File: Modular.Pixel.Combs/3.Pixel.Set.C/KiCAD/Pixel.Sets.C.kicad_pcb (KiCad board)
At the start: 2 copper layers, 78 x 78 mm, 19 parts

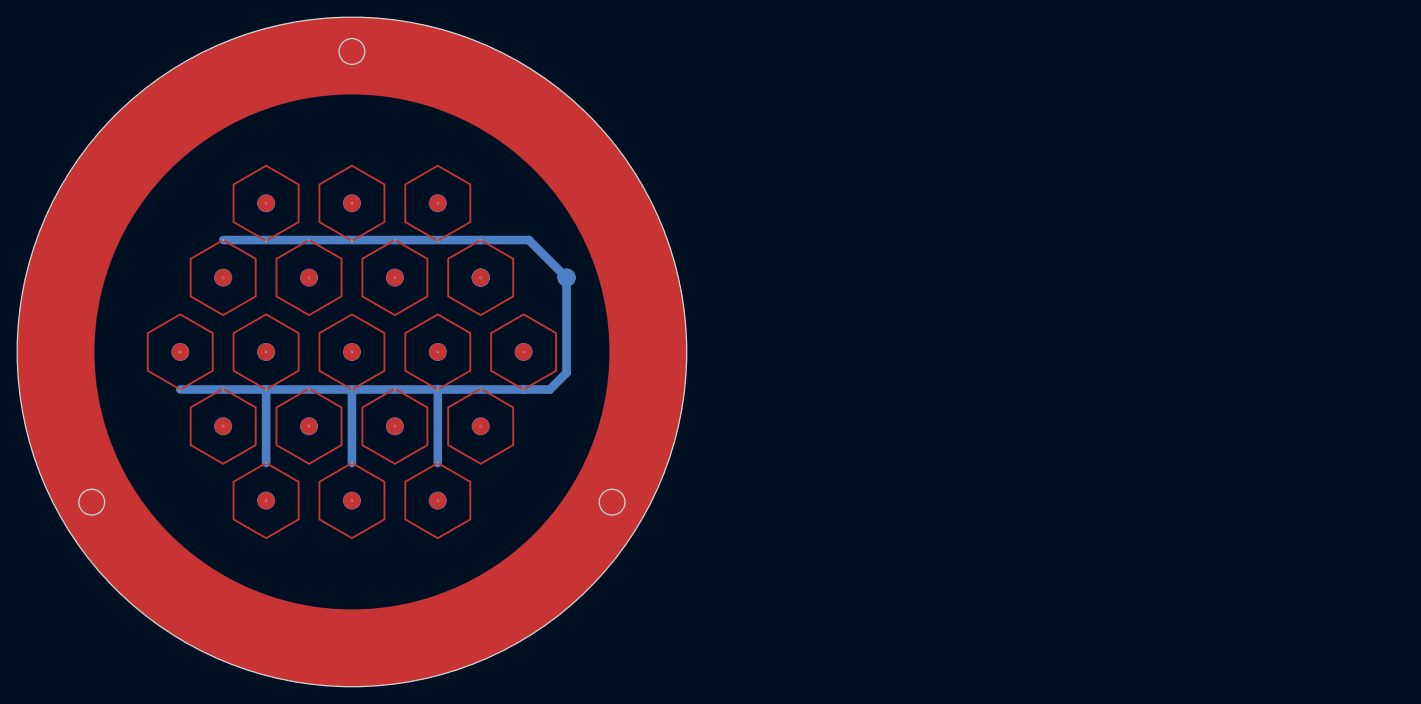
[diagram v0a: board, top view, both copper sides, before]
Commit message: Smoothed out Hexagon Pixels so that it Better Fits the Stencils
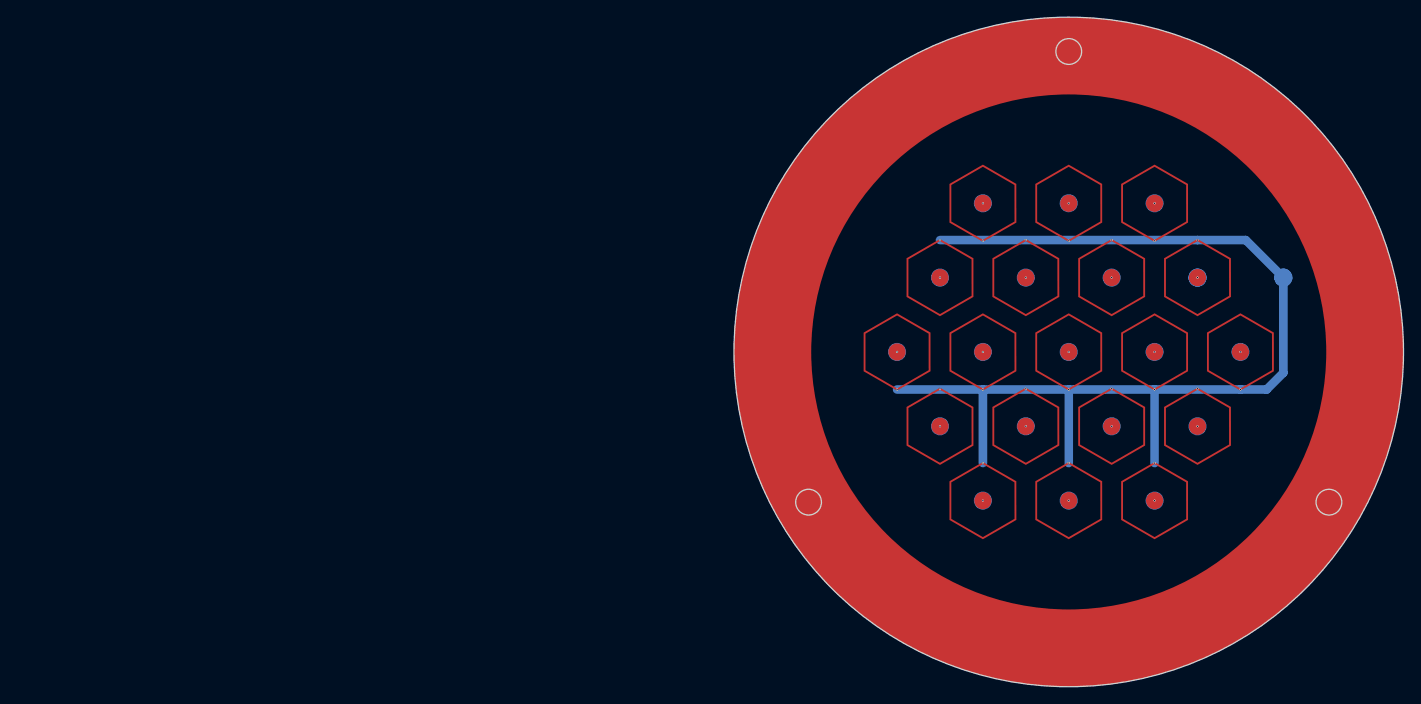
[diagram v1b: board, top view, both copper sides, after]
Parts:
- moved REF** 83.5 mm to (232.0, 58.3)
- moved REF**10 83.5 mm to (237.0, 49.6)
- moved REF**11 83.5 mm to (247.0, 49.6)
- moved REF**13 83.5 mm to (222.0, 41.0)
- moved REF**14 83.5 mm to (232.0, 41.0)
- moved REF**15 83.5 mm to (242.0, 41.0)
- moved REF**3 83.5 mm to (242.0, 58.3)
- moved REF**30 83.5 mm to (237.0, 67.0)
- moved REF**33 83.5 mm to (247.0, 67.0)
- moved REF**38 83.5 mm to (242.0, 75.6)
- moved REF**50 83.5 mm to (212.0, 58.3)
- moved REF**53 83.5 mm to (217.0, 49.6)
- moved REF**6 83.5 mm to (252.0, 58.3)
- moved REF**64 83.5 mm to (222.0, 58.3)
- moved REF**67 83.5 mm to (227.0, 67.0)
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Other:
- board text added: "Pixel Board C ::: May 2023 Alfredo Barajas Enriquez"
- board text removed: "Pixel Set C ::: May 2023 Alfredo Barajas Enriquez"

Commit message: Finalized Pixel Plane Design
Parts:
- removed the REF** at (232.0, 58.3)
- removed REF**10, REF**11, REF**13, REF**14, REF**15, REF**3, REF**30, REF**33, REF**38, REF**50, REF**53, REF**6, REF**64, REF**67, REF**68, REF**71, REF**80, REF**9: Hex.Tile.Solid.G.Dot, Hex:Hex.Tile.Solid.G.Dot
- added REF**: Hex.Tile.Solid.G.Dot, 1.Hex:Hex.Tile.Solid.G.Dot, F.Cu at (222.0, 41.0)
- added REF**: Hex.Tile.Solid.G.Dot, 1.Hex:Hex.Tile.Solid.G.Dot, F.Cu at (252.0, 58.3)
- added REF**: Hex.Tile.Solid.G.Dot, 1.Hex:Hex.Tile.Solid.G.Dot, F.Cu at (247.0, 49.6)
- added REF**: Hex.Tile.Solid.G.Dot, 1.Hex:Hex.Tile.Solid.G.Dot, F.Cu at (242.0, 58.3)
- added REF**: Hex.Tile.Solid.G.Dot, 1.Hex:Hex.Tile.Solid.G.Dot, F.Cu at (212.0, 58.3)
- added REF**: Hex.Tile.Solid.G.Dot, 1.Hex:Hex.Tile.Solid.G.Dot, F.Cu at (237.0, 67.0)
- added REF**: Hex.Tile.Solid.G.Dot, 1.Hex:Hex.Tile.Solid.G.Dot, F.Cu at (242.0, 41.0)
- added REF**: Hex.Tile.Solid.G.Dot, 1.Hex:Hex.Tile.Solid.G.Dot, F.Cu at (227.0, 49.6)
- added REF**: Hex.Tile.Solid.G.Dot, 1.Hex:Hex.Tile.Solid.G.Dot, F.Cu at (232.0, 41.0)
- added REF**: Hex.Tile.Solid.G.Dot, 1.Hex:Hex.Tile.Solid.G.Dot, F.Cu at (222.0, 75.6)
- added REF**: Hex.Tile.Solid.G.Dot, 1.Hex:Hex.Tile.Solid.G.Dot, F.Cu at (222.0, 58.3)
- added REF**: Hex.Tile.Solid.G.Dot, 1.Hex:Hex.Tile.Solid.G.Dot, F.Cu at (217.0, 49.6)
- added REF**: Hex.Tile.Solid.G.Dot, 1.Hex:Hex.Tile.Solid.G.Dot, F.Cu at (232.0, 58.3)
- added REF**: Hex.Tile.Solid.G.Dot, 1.Hex:Hex.Tile.Solid.G.Dot, F.Cu at (232.0, 75.6)
- added REF**: Hex.Tile.Solid.G.Dot, 1.Hex:Hex.Tile.Solid.G.Dot, F.Cu at (237.0, 49.6)
- added REF**: Hex.Tile.Solid.G.Dot, 1.Hex:Hex.Tile.Solid.G.Dot, F.Cu at (227.0, 67.0)
- added REF**: Hex.Tile.Solid.G.Dot, 1.Hex:Hex.Tile.Solid.G.Dot, F.Cu at (242.0, 75.6)
- added REF**: Hex.Tile.Solid.G.Dot, 1.Hex:Hex.Tile.Solid.G.Dot, F.Cu at (247.0, 67.0)
- added REF**: Hex.Tile.Solid.G.Dot, 1.Hex:Hex.Tile.Solid.G.Dot, F.Cu at (217.0, 67.0)

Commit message: Minor Fixes
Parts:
- added G***: LOGO, LOGO, B.Cu at (241.7, 88.2)
